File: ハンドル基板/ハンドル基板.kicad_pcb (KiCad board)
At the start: 2 copper layers, 39.4 x 10.2 mm, 2 parts, among them J1 Conn_01x03

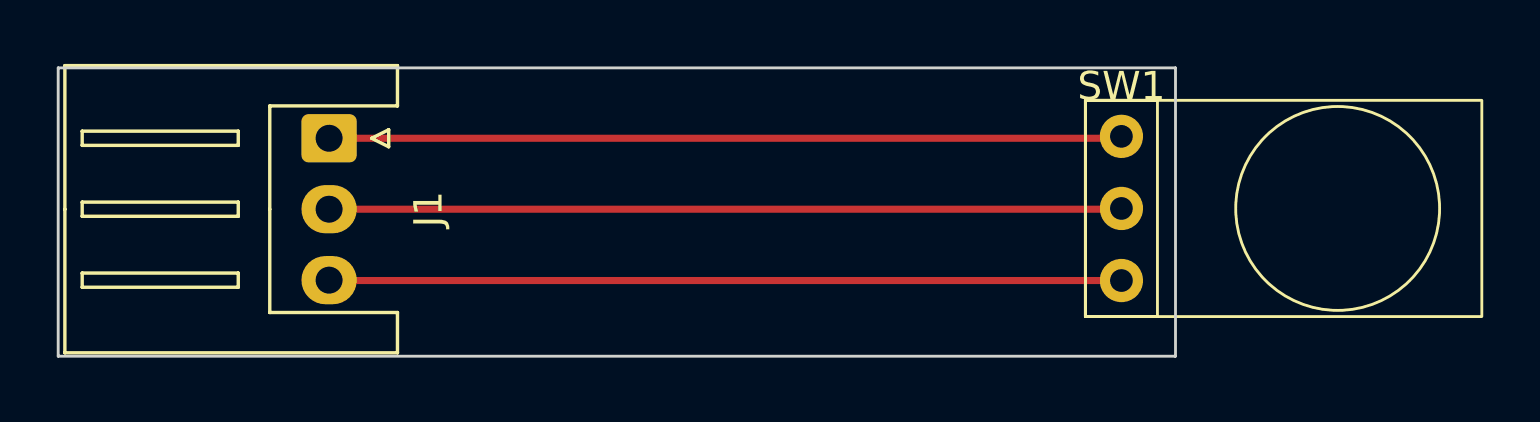
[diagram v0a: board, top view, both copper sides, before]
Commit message: フルカラーLEDロータリーエンコーダDIP変換基板
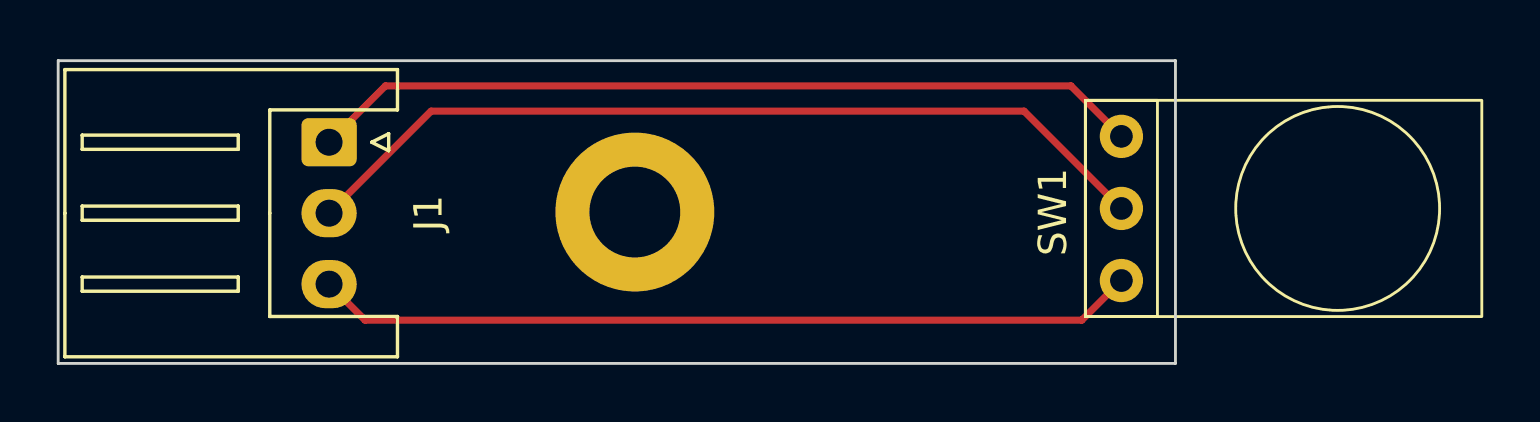
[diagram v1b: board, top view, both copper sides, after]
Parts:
- added REF**: MountingHole_3.2mm_M3_DIN965_Pad, MountingHole:MountingHole_3.2mm_M3_DIN965_Pad, F.Cu at (43.2, 50.8)
- moved J1 0.14 mm to (32.4, 48.3)
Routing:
- net Net-(J1-Pin_2): track 27.9 -> 30.8 mm
- net Net-(J1-Pin_1): track 27.9 -> 29.5 mm
- net Net-(J1-Pin_3): track 27.9 -> 29.0 mm
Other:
- board size 39.4 x 10.2 mm -> 39.4 x 10.7 mm
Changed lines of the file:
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@@
     (property "Sheetname" "")
     (attr through_hole)
-    (fp_text reference "SW1" (at 0 -0.5 unlocked) (layer "F.SilkS")
+    (fp_text reference "SW1" (at -2.413 3.937 90 unlocked) (layer "F.SilkS")
         (effects (font (size 1 1) (thickness 0.1)))
     )
@@
       (net 3 "Net-(J1-Pin_3)") (pinfunction "GND") (pintype "passive"))
   )
+  (footprint "MountingHole:MountingHole_3.2mm_M3_DIN965_Pad" (layer "F.Cu")
+    (at 43.18 50.8)
+    (descr "Mounting Hole 3.2mm, M3, DIN965")
+    (tags "mounting hole 3.2mm m3 din965")
+    (attr exclude_from_pos_files exclude_from_bom)
+    (fp_text reference "REF**" (at 0 -3.8) (layer "F.SilkS") hide
+        (effects (font (size 1 1) (thickness 0.15)))
+    )
+    (fp_text value "MountingHole_3.2mm_M3_DIN965_Pad" (at 0 10.16) (layer "F.Fab")
+        (effects (font (size 1 1) (thickness 0.15)))
+    )
+    (fp_text user "${REFERENCE}" (at 0 0) (layer "F.Fab")
+        (effects (font (size 1 1) (thickness 0.15)))
+    )
+    (fp_circle (center 0 0) (end 2.8 0)
+      (stroke (width 0.15) (type solid)) (fill none) (layer "Cmts.User"))
+    (fp_circle (center 0 0) (end 3.05 0)
+      (stroke (width 0.05) (type solid)) (fill none) (layer "F.CrtYd"))
+    (pad "1" thru_hole circle (at 0 0) (size 5.6 5.6) (drill 3.2) (layers "*.Cu" "*.Mask"))
+  )
   (footprint "Connector_JST:JST_XH_S3B-XH-A_1x03_P2.50mm_Horizontal" (layer "F.Cu")
-    (at 32.406 48.2 -90)
+    (at 32.406 48.34 -90)
     (descr "JST XH series connector, S3B-XH-A (http://www.jst-mfg.com/product/pdf/eng/eXH.pdf), generated with kicad-footprint-generator")
     (tags "connector JST XH horizontal")
@@
     )
   )
-  (gr_rect (start 22.86 45.72) (end 62.23 55.88)
+  (gr_rect (start 22.86 45.466) (end 62.23 56.134)
     (stroke (width 0.1) (type default)) (fill none) (layer "Edge.Cuts"))
   (dimension (type aligned) (layer "Eco1.User")
@@
     (style (thickness 0.15) (arrow_length 1.27) (text_position_mode 0) (extension_height 0.58642) (extension_offset 0.5) keep_text_aligned)
   )
-  (segment (start 60.258 48.2) (end 60.325 48.133) (width 0.25) (layer "F.Cu") (net 1))
-  (segment (start 32.406 48.2) (end 60.258 48.2) (width 0.25) (layer "F.Cu") (net 1))
-  (segment (start 32.406 50.7) (end 60.298 50.7) (width 0.25) (layer "F.Cu") (net 2))
-  (segment (start 60.298 50.7) (end 60.325 50.673) (width 0.25) (layer "F.Cu") (net 2))
-  (segment (start 32.419 53.213) (end 32.406 53.2) (width 0.25) (layer "F.Cu") (net 3))
-  (segment (start 60.325 53.213) (end 32.419 53.213) (width 0.25) (layer "F.Cu") (net 3))
+  (segment (start 32.406 48.34) (end 34.391 46.355) (width 0.25) (layer "F.Cu") (net 1))
+  (segment (start 34.391 46.355) (end 58.547 46.355) (width 0.25) (layer "F.Cu") (net 1))
+  (segment (start 58.547 46.355) (end 60.325 48.133) (width 0.25) (layer "F.Cu") (net 1))
+  (segment (start 56.896 47.244) (end 60.325 50.673) (width 0.25) (layer "F.Cu") (net 2))
+  (segment (start 36.002 47.244) (end 56.896 47.244) (width 0.25) (layer "F.Cu") (net 2))
+  (segment (start 32.406 50.84) (end 36.002 47.244) (width 0.25) (layer "F.Cu") (net 2))
+  (segment (start 33.676 54.61) (end 58.928 54.61) (width 0.25) (layer "F.Cu") (net 3))
+  (segment (start 32.406 53.34) (end 33.676 54.61) (width 0.25) (layer "F.Cu") (net 3))
+  (segment (start 58.928 54.61) (end 60.325 53.213) (width 0.25) (layer "F.Cu") (net 3))
 )
